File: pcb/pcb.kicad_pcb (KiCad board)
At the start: 2 copper layers, 23 parts, among them J1 USB_B_Micro, J2 AVR ISP connector, J3 Display connector, SW1 SW_DPDT_x2, SW2 SW_DIP_x01, SW3 SW_DIP_x01, U1 ATmega328P-AU, U2 MCP73831-2-OT, U3 AP9101CK6, U4 DMN2053UVT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

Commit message: Finalized PCB layout
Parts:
- removed R4, R6: 10K, Resistor_SMD:R_0603_1608Metric
- added C5: 100n, Capacitor_SMD:C_0603_1608Metric, F.Cu at (14.5, 6.00)
- added C6: 100n, Capacitor_SMD:C_0603_1608Metric, F.Cu at (26.0, 21.2)
- added J4: Conn_01x02_Male, Connector_JST:JST_PH_B2B-PH-K_1x02_P2.00mm_Vertical, F.Cu at (24.5, 33.5)
- added REF**: MOUNTING_HOLE, pcb:MOUNTING_HOLE, F.Cu at (32.0, 32.5)
- added REF**: MOUNTING_HOLE, pcb:MOUNTING_HOLE, F.Cu at (3.00, 32.5)
- added REF**: MOUNTING_HOLE, pcb:MOUNTING_HOLE, F.Cu at (32.0, 3.00)
- added REF**: MOUNTING_HOLE, pcb:MOUNTING_HOLE, F.Cu at (3.00, 3.00)
- added REF**: Adafruit_SSD1306_No_Mounting_Holes, Display:Adafruit_SSD1306_No_Mounting_Holes, F.Cu at (49.7, 3.90)
- SW1: value SW_DPDT_x2 -> SSSS811101; footprint pcb:SW_3P -> pcb:SSSS811101
- moved C1 145.4 mm to (7.21, 30.0), turned to 180 degrees
- moved R2 139.9 mm to (23.2, 9.25), turned to 180 degrees
- moved R7 139.0 mm to (14.2, 27.0), turned to 180 degrees
- moved U3 138.5 mm to (16.5, 23.8), turned to 270 degrees
- moved C2 137.8 mm to (15.2, 19.5)
- moved R1 137.6 mm to (16.7, 32.8), turned to 180 degrees
- moved R5 137.4 mm to (20.2, 24.8), turned to 90 degrees
- moved R3 136.2 mm to (14.2, 29.5), turned to 180 degrees
- moved U4 135.0 mm to (11.5, 23.8), turned to 90 degrees
- moved C4 134.1 mm to (22.8, 24.7), turned to 270 degrees
- moved U1 129.8 mm to (14.8, 12.8), turned to 270 degrees
- moved C3 128.8 mm to (22.8, 29.3), turned to 270 degrees
- moved U5 127.0 mm to (24.4, 16.0), turned to 90 degrees
- moved SW2 125.3 mm to (34.0, 16.0), turned to 90 degrees
- moved SW3 122.7 mm to (34.0, 9.25), turned to 90 degrees
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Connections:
- J1 pad 6: Net-(J1-Pad6) -> GND
- U1 pad 20: Net-(U1-Pad20) -> VCC
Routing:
- net VCC: track 0.00 -> 87.0 mm, vias 0 -> 5
- net BAT+: track 0.00 -> 30.5 mm
- net BAT-: track 0.00 -> 30.3 mm, vias 0 -> 2
- net RESET: track 0.00 -> 24.4 mm, vias 0 -> 3
- net SDA: track 0.00 -> 24.2 mm, vias 0 -> 1
- net Net-(C1-Pad1): track 0.00 -> 20.8 mm
- net SCL: track 0.00 -> 19.2 mm, vias 0 -> 1
- net BTN1: track 0.00 -> 17.4 mm, vias 0 -> 2
- net BTN2: track 0.00 -> 15.8 mm, vias 0 -> 2
- net DISP_RST: track 0.00 -> 13.3 mm
- net GND: track 0.00 -> 12.9 mm, vias 0 -> 4
- net SCK: track 0.00 -> 12.3 mm, vias 0 -> 3
- net MISO: track 0.00 -> 8.38 mm, vias 0 -> 1
- net MOSI: track 0.00 -> 8.34 mm, vias 0 -> 1
- net Net-(R1-Pad2): track 0.00 -> 5.71 mm
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- added copper zone on B.Cu, net GND
- added copper zone on F.Cu, net GND
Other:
- board outline added: 35 x 37 mm

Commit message: Finalized schematic and PCB layout
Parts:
- moved REF** 20.2 mm to (69.8, 5.50)
- moved C1 8.12 mm to (15.3, 29.3), turned to 270 degrees
- moved C6 5.65 mm to (28.1, 16.0), turned to 90 degrees
- moved R3 3.85 mm to (16.0, 32.9)
- moved R1 2.39 mm to (19.1, 32.6), turned to 90 degrees
- moved R7 2.12 mm to (12.1, 27.0)
- moved D1 0.26 mm to (16.8, 35.5)
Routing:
- net GND: track 12.9 -> 4.70 mm, vias 4 -> 3
- net BAT+: track 30.5 -> 35.6 mm
- net Net-(R1-Pad2): track 5.71 -> 2.42 mm
- net Net-(R7-Pad1): track 4.80 -> 6.92 mm
- net BTN1: track 17.4 -> 18.2 mm
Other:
- board text added: "+"
- board text added: "-"

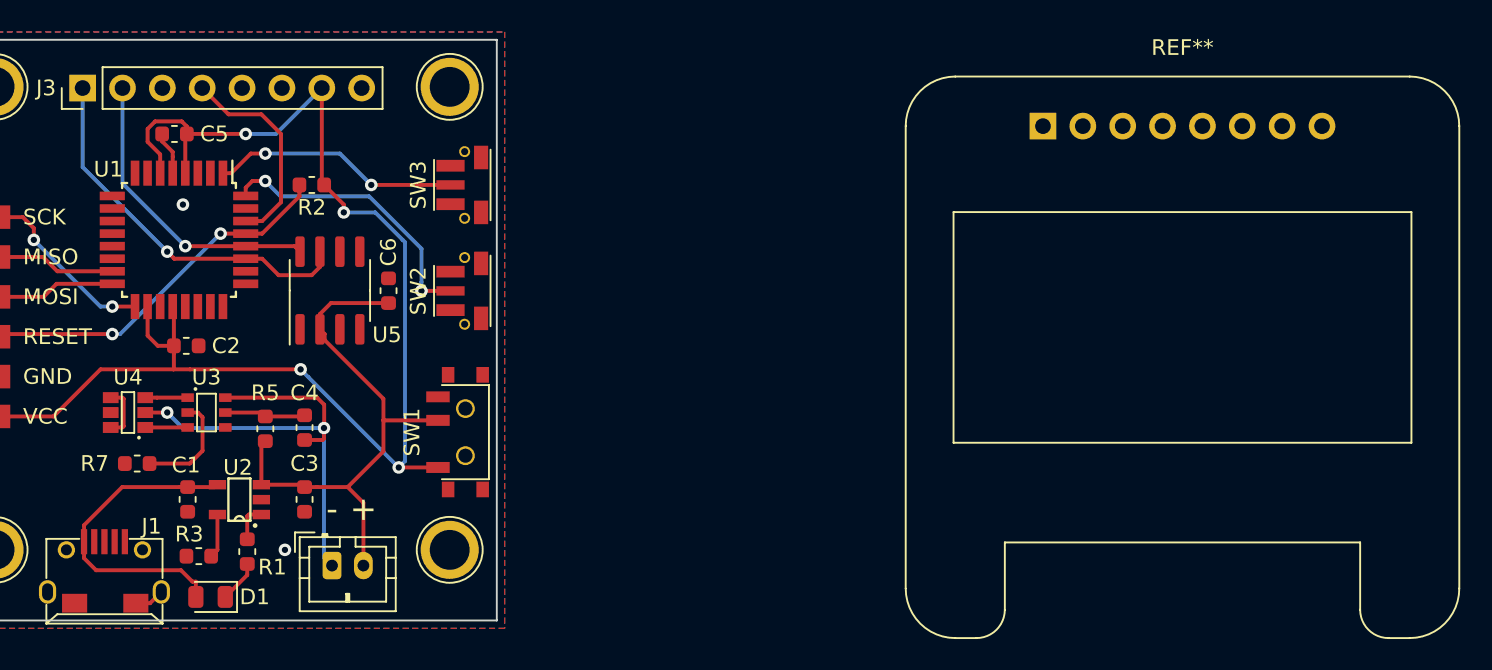
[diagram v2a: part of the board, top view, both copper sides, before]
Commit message: Changed TL3340 footprint
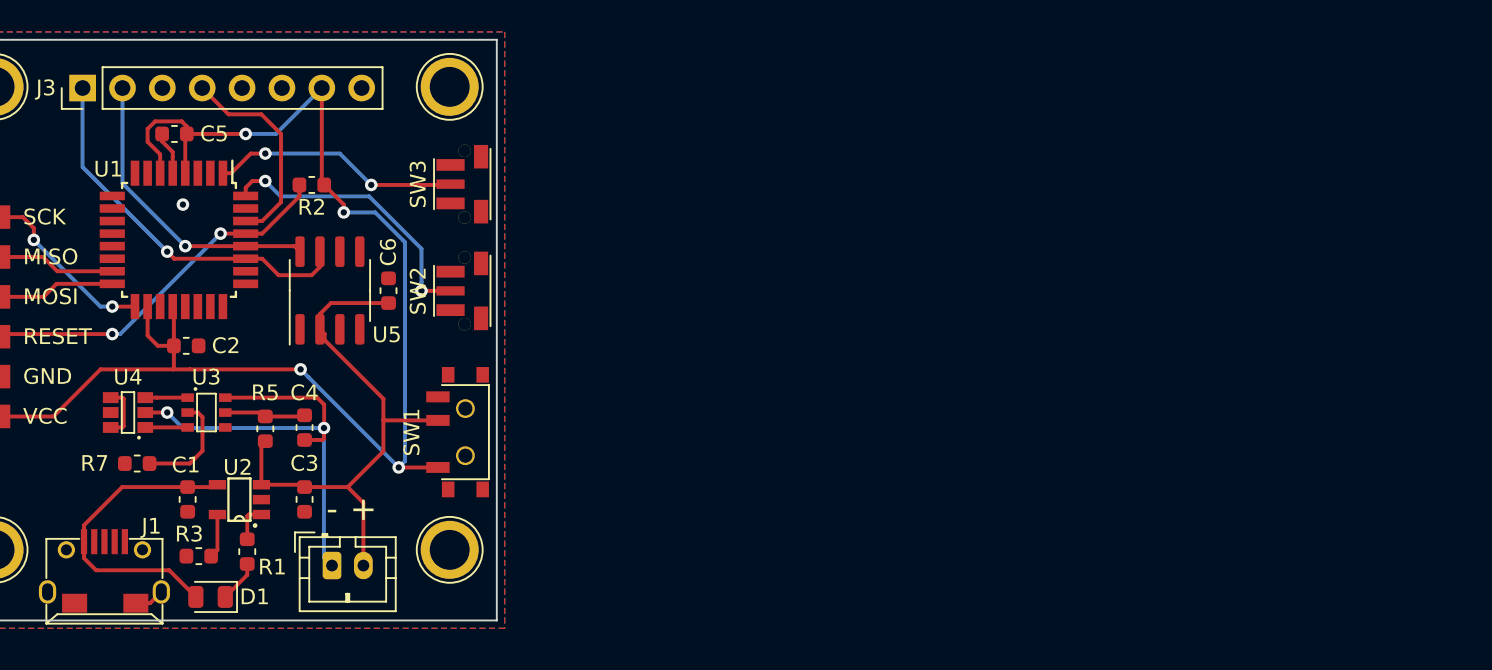
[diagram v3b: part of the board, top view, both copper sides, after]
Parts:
- removed the REF** at (69.8, 5.50)
- moved SW3 0.05 mm to (34.0, 9.20)
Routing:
- net Net-(C1-Pad1): track 20.4 -> 19.8 mm
- net GND: vias 3 -> 2
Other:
- board text added: "AVRist-Watch by Florian Winkler Revision 1 https://github.com/Fju/AVRist-watch"

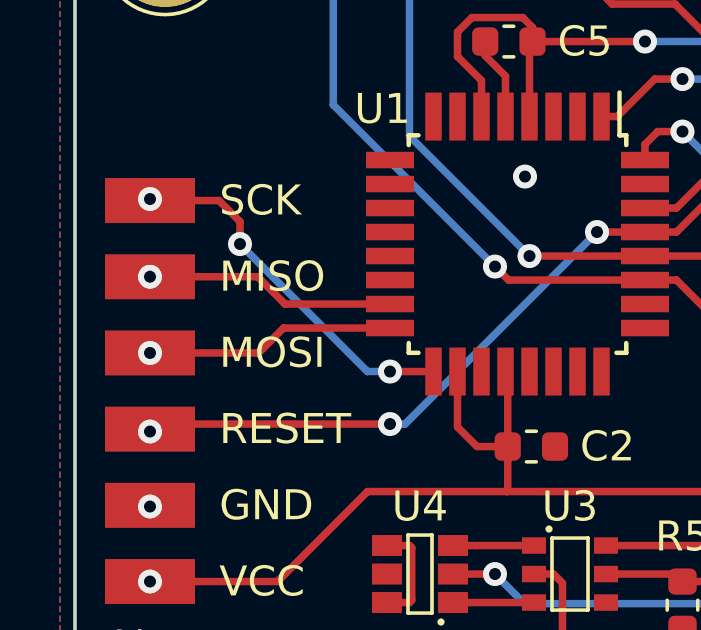
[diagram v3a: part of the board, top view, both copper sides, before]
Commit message: Fixed MISO/MOSI mistake in PCB and schematic
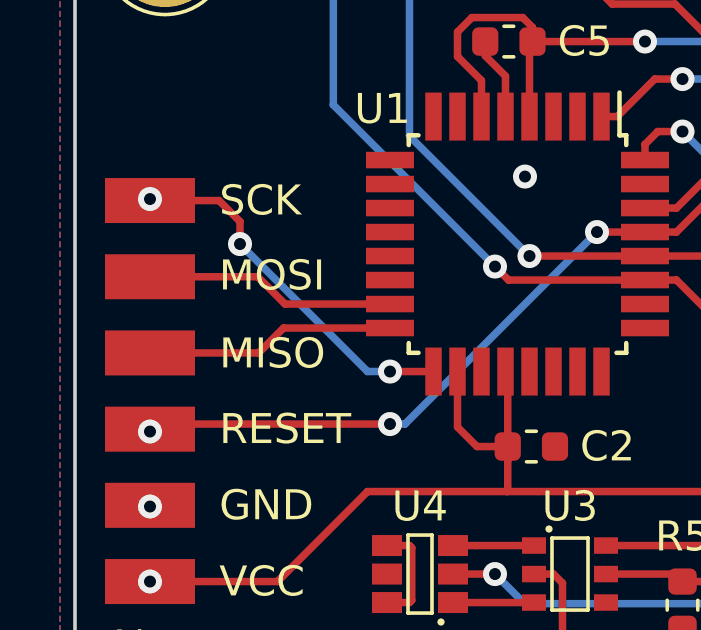
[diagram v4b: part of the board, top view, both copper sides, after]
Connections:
- J2 pad 4: MOSI -> MISO
- J2 pad 5: MISO -> MOSI
- U1 pad 15: MISO -> MOSI
- U1 pad 16: MOSI -> MISO
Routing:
- net MOSI: track 8.34 -> 8.38 mm, vias 1 -> 0
- net MISO: track 8.38 -> 8.34 mm, vias 1 -> 0
